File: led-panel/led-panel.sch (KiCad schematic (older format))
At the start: 34 parts, among them J1 Conn_01x04, J2 Conn_01x08

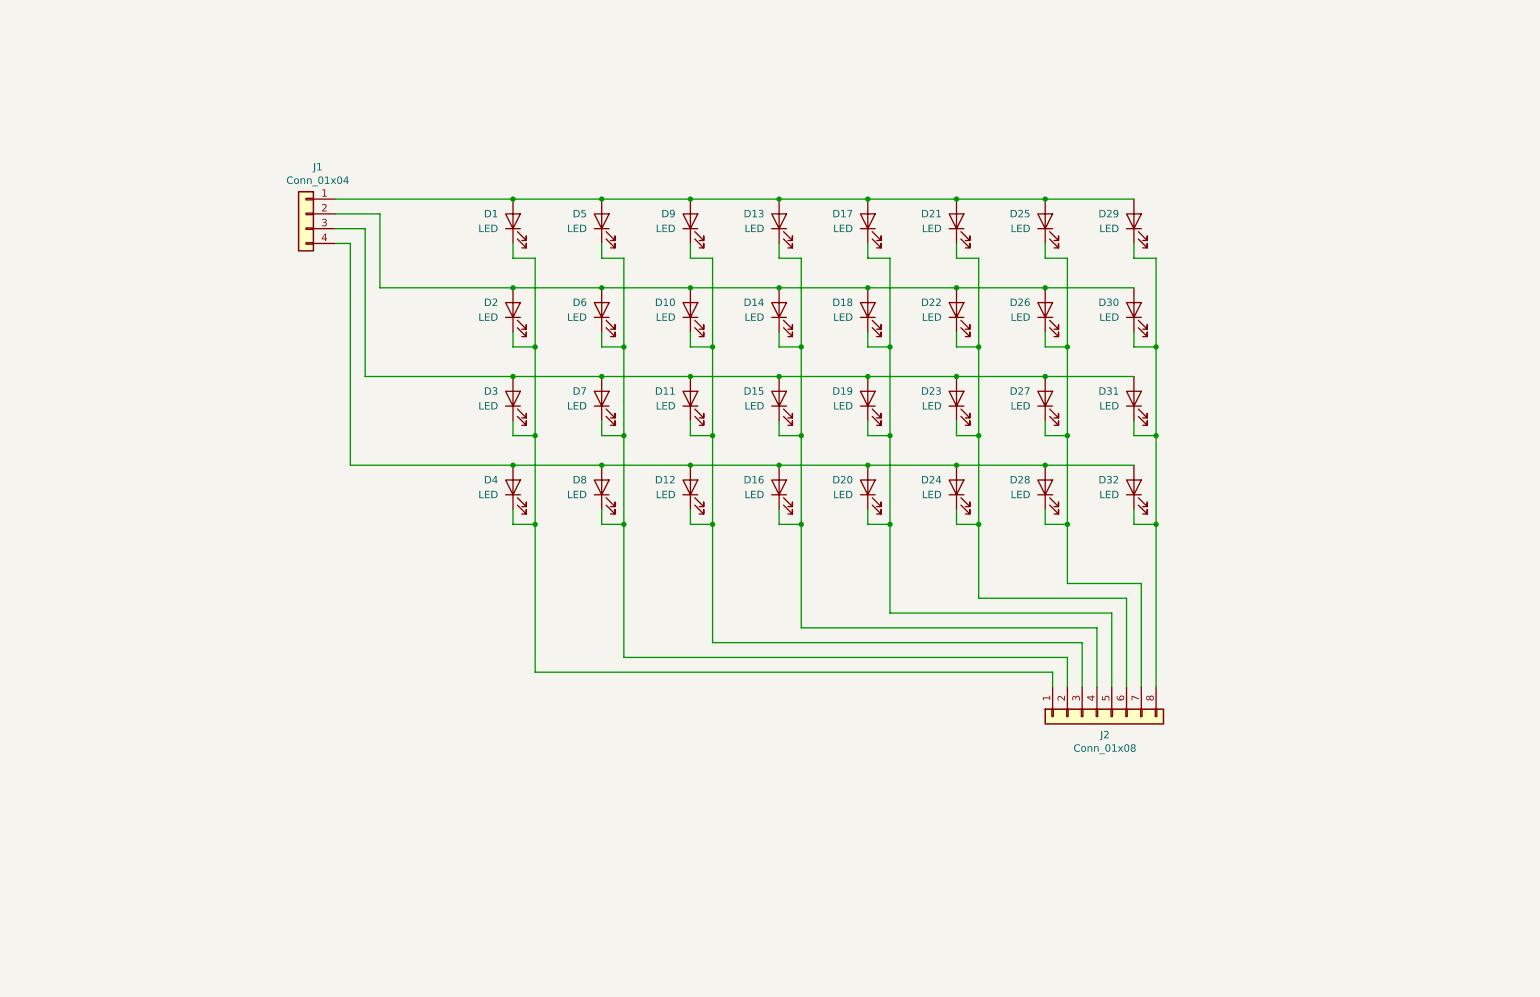
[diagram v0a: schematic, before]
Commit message: schematic for an 8x16 panel
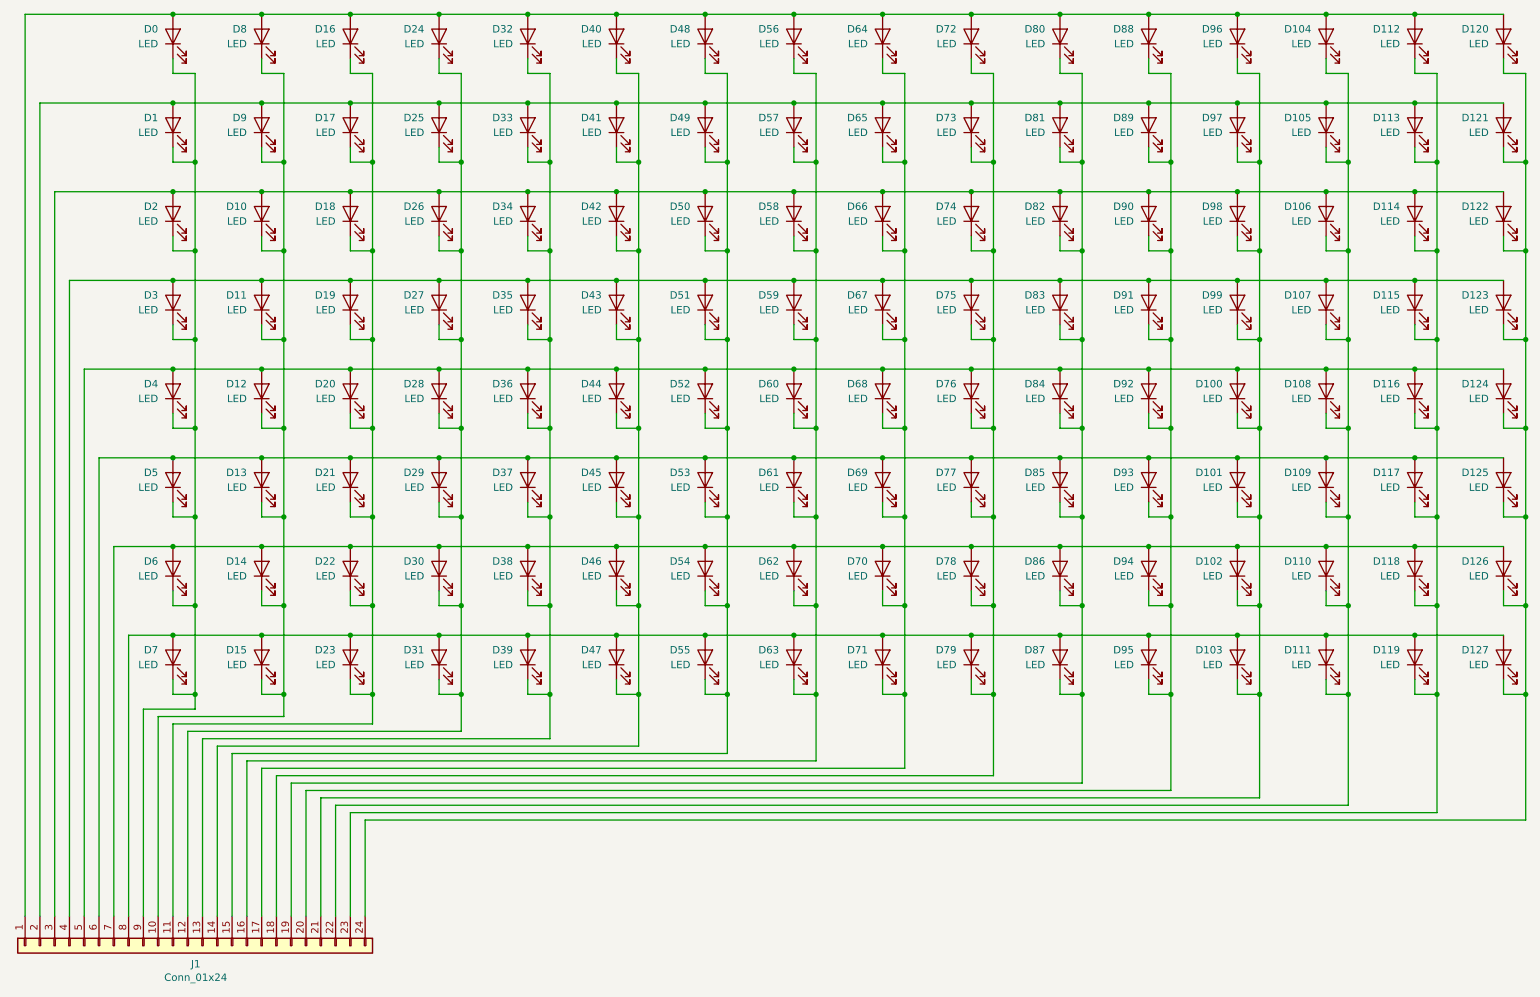
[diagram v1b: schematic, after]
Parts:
- removed J1: Conn_01x04, Connector_PinHeader_2.54mm:PinHeader_1x04_P2.54mm_Vertical, symbol Connector_Generic:Conn_01x04
- removed J2: Conn_01x08, Connector_PinHeader_2.54mm:PinHeader_1x08_P2.54mm_Vertical, symbol Connector_Generic:Conn_01x08
- added D100, D101, D102, D103, D104, D105, D106, D107, D108, D109, D110, D111, D112, D113, D114, D115, D116, D117, D118, D119, D12, D120, D121, D122, D123, D124, D125, D126, D127, D13, D14, D15, D20, D21, D22, D23, D28, D29, D30, D31, D36, D37, D38, D39, D4, D44, D45, D46, D47, D5, D52, D53, D54, D55, D6, D60, D61, D62, D63, D64, D65, D66, D67, D68, D69, D7, D70, D71, D72, D73, D74, D75, D76, D77, D78, D79, D80, D81, D82, D83, D84, D85, D86, D87, D88, D89, D90, D91, D92, D93, D94, D95, D96, D97, D98, D99: LED, LED_THT:LED_D3.0mm, symbol Device:LED
- added J1: Conn_01x24, Connector_PinHeader_2.54mm:PinHeader_1x24_P2.54mm_Vertical, symbol Connector_Generic:Conn_01x24
- D0: renamed from D1; footprint Diode_SMD:D_0805_2012Metric_Castellated -> LED_THT:LED_D3.0mm
- D1: renamed from D2; footprint Diode_SMD:D_0805_2012Metric_Castellated -> LED_THT:LED_D3.0mm
- D10: renamed from D7; footprint Diode_SMD:D_0805_2012Metric_Castellated -> LED_THT:LED_D3.0mm
- D11: renamed from D8; footprint Diode_SMD:D_0805_2012Metric_Castellated -> LED_THT:LED_D3.0mm
- D16: renamed from D9; footprint Diode_SMD:D_0805_2012Metric_Castellated -> LED_THT:LED_D3.0mm
- D17: renamed from D10; footprint Diode_SMD:D_0805_2012Metric_Castellated -> LED_THT:LED_D3.0mm
- D18: renamed from D11; footprint Diode_SMD:D_0805_2012Metric_Castellated -> LED_THT:LED_D3.0mm
- D19: renamed from D12; footprint Diode_SMD:D_0805_2012Metric_Castellated -> LED_THT:LED_D3.0mm
- D2: renamed from D3; footprint Diode_SMD:D_0805_2012Metric_Castellated -> LED_THT:LED_D3.0mm
- D24: renamed from D13; footprint Diode_SMD:D_0805_2012Metric_Castellated -> LED_THT:LED_D3.0mm
- D25: renamed from D14; footprint Diode_SMD:D_0805_2012Metric_Castellated -> LED_THT:LED_D3.0mm
- D26: renamed from D15; footprint Diode_SMD:D_0805_2012Metric_Castellated -> LED_THT:LED_D3.0mm
- D27: renamed from D16; footprint Diode_SMD:D_0805_2012Metric_Castellated -> LED_THT:LED_D3.0mm
- D3: renamed from D4; footprint Diode_SMD:D_0805_2012Metric_Castellated -> LED_THT:LED_D3.0mm
- D32: renamed from D17; footprint Diode_SMD:D_0805_2012Metric_Castellated -> LED_THT:LED_D3.0mm
- D33: renamed from D18; footprint Diode_SMD:D_0805_2012Metric_Castellated -> LED_THT:LED_D3.0mm
- D34: renamed from D19; footprint Diode_SMD:D_0805_2012Metric_Castellated -> LED_THT:LED_D3.0mm
- D35: renamed from D20; footprint Diode_SMD:D_0805_2012Metric_Castellated -> LED_THT:LED_D3.0mm
- D40: renamed from D21; footprint Diode_SMD:D_0805_2012Metric_Castellated -> LED_THT:LED_D3.0mm
- D41: renamed from D22; footprint Diode_SMD:D_0805_2012Metric_Castellated -> LED_THT:LED_D3.0mm
- D42: renamed from D23; footprint Diode_SMD:D_0805_2012Metric_Castellated -> LED_THT:LED_D3.0mm
- D43: renamed from D24; footprint Diode_SMD:D_0805_2012Metric_Castellated -> LED_THT:LED_D3.0mm
- D48: renamed from D25; footprint Diode_SMD:D_0805_2012Metric_Castellated -> LED_THT:LED_D3.0mm
- D49: renamed from D26; footprint Diode_SMD:D_0805_2012Metric_Castellated -> LED_THT:LED_D3.0mm
- D50: renamed from D27; footprint Diode_SMD:D_0805_2012Metric_Castellated -> LED_THT:LED_D3.0mm
- D51: renamed from D28; footprint Diode_SMD:D_0805_2012Metric_Castellated -> LED_THT:LED_D3.0mm
- D56: renamed from D29; footprint Diode_SMD:D_0805_2012Metric_Castellated -> LED_THT:LED_D3.0mm
- D57: renamed from D30; footprint Diode_SMD:D_0805_2012Metric_Castellated -> LED_THT:LED_D3.0mm
- D58: renamed from D31; footprint Diode_SMD:D_0805_2012Metric_Castellated -> LED_THT:LED_D3.0mm
- D59: renamed from D32; footprint Diode_SMD:D_0805_2012Metric_Castellated -> LED_THT:LED_D3.0mm
- D8: renamed from D5; footprint Diode_SMD:D_0805_2012Metric_Castellated -> LED_THT:LED_D3.0mm
- D9: renamed from D6; footprint Diode_SMD:D_0805_2012Metric_Castellated -> LED_THT:LED_D3.0mm
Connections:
- net at D0.1 (K), D1.1 (K), D2.1 (K)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: now also D4.1 (K), D5.1 (K), D6.1 (K), D7.1 (K), J1.9 (Pin_9)
- net at D0.2 (A), D16.2 (A), D24.2 (A)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: now also D104.2 (A), D112.2 (A), D120.2 (A), D64.2 (A), D72.2 (A), D80.2 (A), D88.2 (A), D96.2 (A), J1.1 (Pin_1)
- net at D1.2 (A), D17.2 (A), D25.2 (A)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: now also D105.2 (A), D113.2 (A), D121.2 (A), D65.2 (A), D73.2 (A), D81.2 (A), D89.2 (A), D97.2 (A), J1.2 (Pin_2)
- net at D10.2 (A), D18.2 (A), D2.2 (A)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: now also D106.2 (A), D114.2 (A), D122.2 (A), D66.2 (A), D74.2 (A), D82.2 (A), D90.2 (A), D98.2 (A), J1.3 (Pin_3)
- net at D11.2 (A), D19.2 (A), D27.2 (A)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: now also D107.2 (A), D115.2 (A), D123.2 (A), D67.2 (A), D75.2 (A), D83.2 (A), D91.2 (A), D99.2 (A), J1.4 (Pin_4)
- net at D10.1 (K), D11.1 (K), D8.1 (K)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: now also D12.1 (K), D13.1 (K), D14.1 (K), D15.1 (K), J1.10 (Pin_10)
- net at D16.1 (K), D17.1 (K), D18.1 (K)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: now also D20.1 (K), D21.1 (K), D22.1 (K), D23.1 (K), J1.11 (Pin_11)
- net at D24.1 (K), D25.1 (K), D26.1 (K)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: now also D28.1 (K), D29.1 (K), D30.1 (K), D31.1 (K), J1.12 (Pin_12)
- net at D32.1 (K), D33.1 (K), D34.1 (K)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: now also D36.1 (K), D37.1 (K), D38.1 (K), D39.1 (K), J1.13 (Pin_13)
- net at D40.1 (K), D41.1 (K), D42.1 (K)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: now also D44.1 (K), D45.1 (K), D46.1 (K), D47.1 (K), J1.14 (Pin_14)
- net at D48.1 (K), D49.1 (K), D50.1 (K)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: now also D52.1 (K), D53.1 (K), D54.1 (K), D55.1 (K), J1.15 (Pin_15)
- net at D56.1 (K), D57.1 (K), D58.1 (K)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: now also D60.1 (K), D61.1 (K), D62.1 (K), D63.1 (K), J1.16 (Pin_16)
- new net: D100.2 (A), D108.2 (A), D116.2 (A), D12.2 (A), D124.2 (A), D20.2 (A), D28.2 (A), D36.2 (A), D4.2 (A), D44.2 (A), D52.2 (A), D60.2 (A), D68.2 (A), D76.2 (A), D84.2 (A), D92.2 (A), J1.5 (Pin_5)
- new net: D101.2 (A), D109.2 (A), D117.2 (A), D125.2 (A), D13.2 (A), D21.2 (A), D29.2 (A), D37.2 (A), D45.2 (A), D5.2 (A), D53.2 (A), D61.2 (A), D69.2 (A), D77.2 (A), D85.2 (A), D93.2 (A), J1.6 (Pin_6)
- new net: D102.2 (A), D110.2 (A), D118.2 (A), D126.2 (A), D14.2 (A), D22.2 (A), D30.2 (A), D38.2 (A), D46.2 (A), D54.2 (A), D6.2 (A), D62.2 (A), D70.2 (A), D78.2 (A), D86.2 (A), D94.2 (A), J1.7 (Pin_7)
- new net: D103.2 (A), D111.2 (A), D119.2 (A), D127.2 (A), D15.2 (A), D23.2 (A), D31.2 (A), D39.2 (A), D47.2 (A), D55.2 (A), D63.2 (A), D7.2 (A), D71.2 (A), D79.2 (A), D87.2 (A), D95.2 (A), J1.8 (Pin_8)
- new net: D64.1 (K), D65.1 (K), D66.1 (K), D67.1 (K), D68.1 (K), D69.1 (K), D70.1 (K), D71.1 (K), J1.17 (Pin_17)
- new net: D72.1 (K), D73.1 (K), D74.1 (K), D75.1 (K), D76.1 (K), D77.1 (K), D78.1 (K), D79.1 (K), J1.18 (Pin_18)
- new net: D80.1 (K), D81.1 (K), D82.1 (K), D83.1 (K), D84.1 (K), D85.1 (K), D86.1 (K), D87.1 (K), J1.19 (Pin_19)
- new net: D88.1 (K), D89.1 (K), D90.1 (K), D91.1 (K), D92.1 (K), D93.1 (K), D94.1 (K), D95.1 (K), J1.20 (Pin_20)
- new net: D100.1 (K), D101.1 (K), D102.1 (K), D103.1 (K), D96.1 (K), D97.1 (K), D98.1 (K), D99.1 (K), J1.21 (Pin_21)
- new net: D104.1 (K), D105.1 (K), D106.1 (K), D107.1 (K), D108.1 (K), D109.1 (K), D110.1 (K), D111.1 (K), J1.22 (Pin_22)
- new net: D112.1 (K), D113.1 (K), D114.1 (K), D115.1 (K), D116.1 (K), D117.1 (K), D118.1 (K), D119.1 (K), J1.23 (Pin_23)
- new net: D120.1 (K), D121.1 (K), D122.1 (K), D123.1 (K), D124.1 (K), D125.1 (K), D126.1 (K), D127.1 (K), J1.24 (Pin_24)
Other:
- moved on the sheet: D0, D1, D10, D11, D16, D17, D18, D19, D2, D24, D25, D26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

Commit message: update header footprint silkscreen
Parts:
- J1: footprint Connector_PinHeader_2.54mm:PinHeader_1x24_P2.54mm_Vertical -> led-panel:PinHeader_1x8+16_P2.54mm_Vertical
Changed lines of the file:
@@
 EESchema Schematic File Version 4
+LIBS:led-panel-cache
 EELAYER 26 0
 EELAYER END
@@
 F 0 "J1" V 1974 7096 50  0000 C CNN
 F 1 "Conn_01x24" V 2065 7096 50  0000 C CNN
-F 2 "Connector_PinHeader_2.54mm:PinHeader_1x24_P2.54mm_Vertical" H 1850 7150 50  0001 C CNN
+F 2 "led-panel:PinHeader_1x8+16_P2.54mm_Vertical" H 1850 7150 50  0001 C CNN
 F 3 "~" H 1850 7150 50  0001 C CNN
 	1    1850 7150

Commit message: fix led silkscreen
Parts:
- D0, D1, D10, D100, D101, D102, D103, D104, D105, D106, D107, D108, D109, D11, D110, D111, D112, D113, D114, D115, D116, D117, D118, D119, D12, D120, D121, D122, D123, D124, D125, D126, D127, D13, D14, D15, D16, D17, D18, D19, D2, D20, D21, D22, D23, D24, D25, D26, D27, D28, D29, D3, D30, D31, D32, D33, D34, D35, D36, D37, D38, D39, D4, D40, D41, D42, D43, D44, D45, D46, D47, D48, D49, D5, D50, D51, D52, D53, D54, D55, D56, D57, D58, D59, D6, D60, D61, D62, D63, D64, D65, D66, D67, D68, D69, D7, D70, D71, D72, D73, D74, D75, D76, D77, D78, D79, D8, D80, D81, D82, D83, D84, D85, D86, D87, D88, D89, D9, D90, D91, D92, D93, D94, D95, D96, D97, D98, D99: footprint LED_THT:LED_D3.0mm -> led-panel:LED_D3.0mm
